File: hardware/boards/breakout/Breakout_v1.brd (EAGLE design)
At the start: 42 x 42 mm, 4 parts

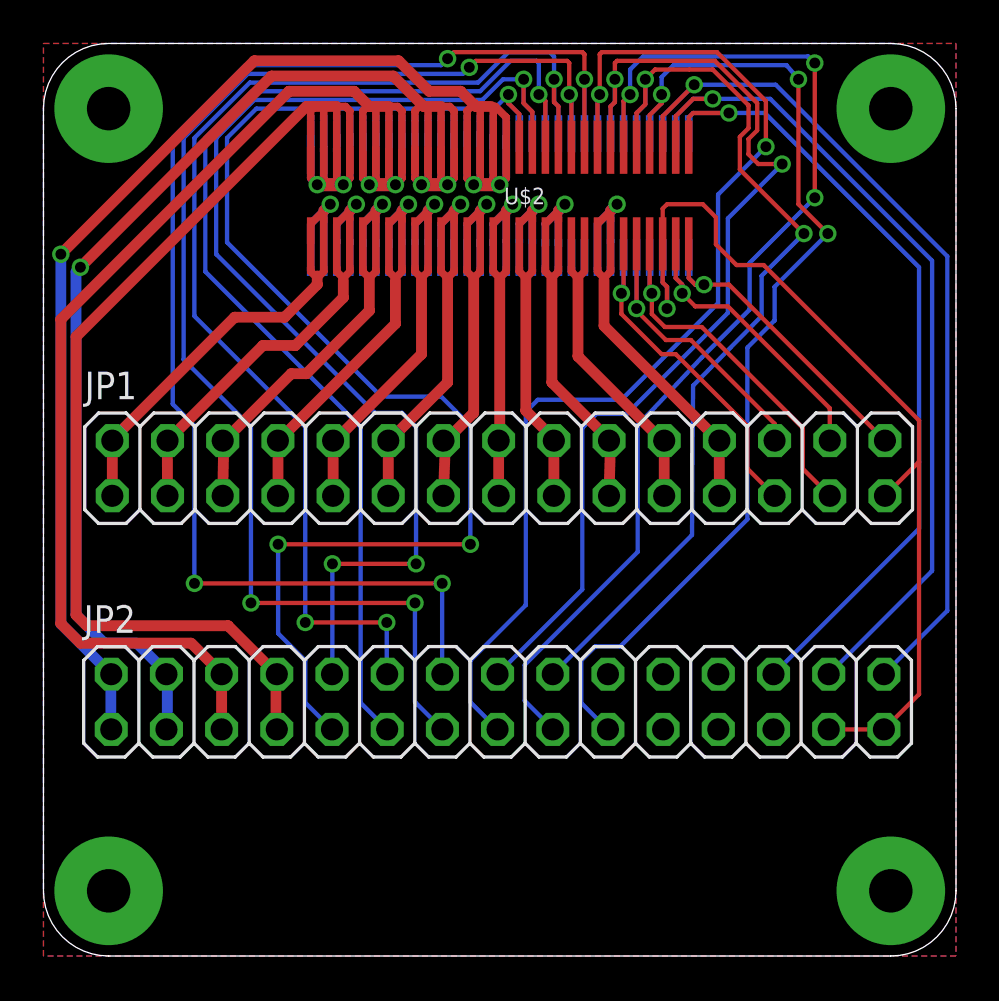
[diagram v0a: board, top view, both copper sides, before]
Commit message: Added V2 breakout ready to order
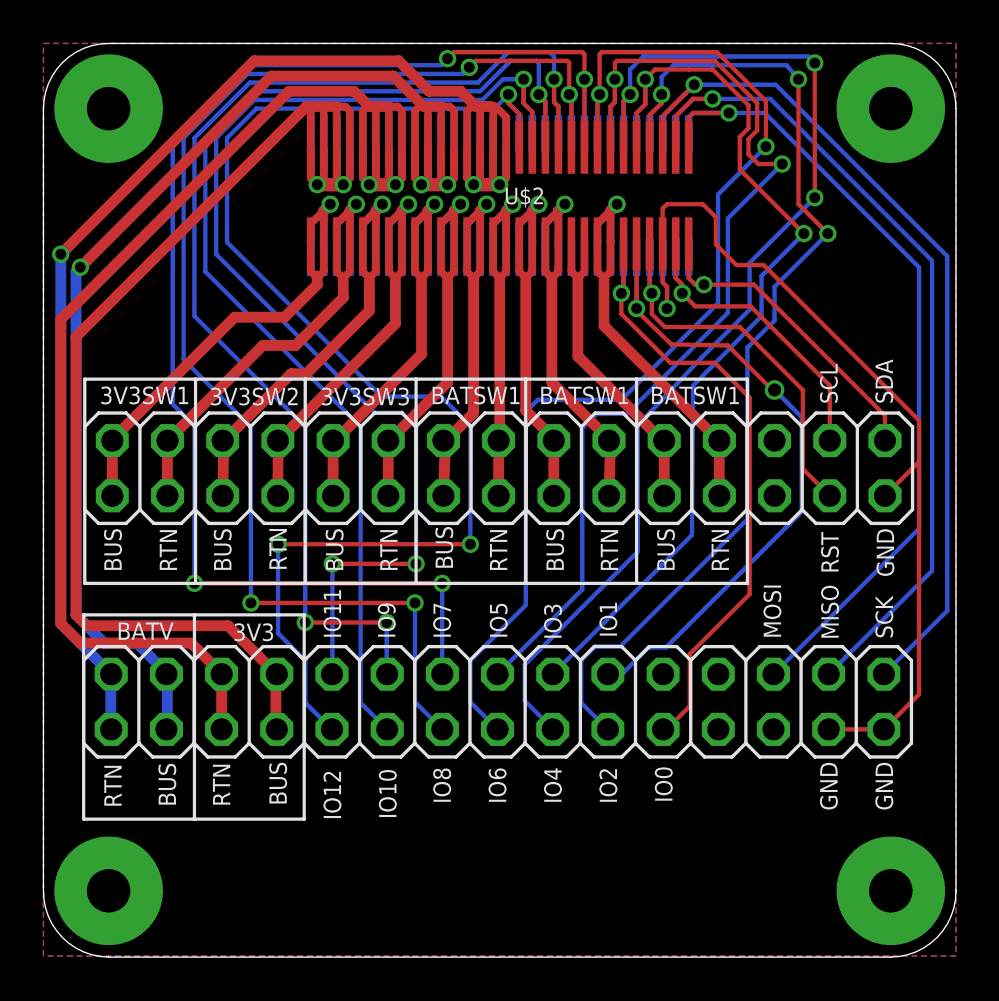
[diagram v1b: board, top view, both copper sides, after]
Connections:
- removed net N$33: JP2.21
- removed net N$43: JP2.20
- net GPIO0: now also JP2.21; no longer JP1.25
- net GPIO1: now also JP2.20; no longer JP1.26
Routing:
- net GPIO1: track 14.7 -> 31.4 mm, vias 1 -> 2
- net GPIO0: track 16.6 -> 29.5 mm
- net /RST: track 17.7 -> 18.7 mm
- net SDA: track 14.5 -> 15.1 mm
- net SCL: track 13.3 -> 13.9 mm
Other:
- board text added: "3V3"
- board text added: "3V3SW1"
- board text added: "3V3SW2"
- board text added: "3V3SW3"
- board text added: "BATSW1"
- board text added: "BATV"
- board text added: "BUS"
- board text added: "GND"
- board text added: "IO0"
- board text added: "IO1"
- board text added: "IO10"
- board text added: "IO11"
- board text added: "IO12"
- board text added: "IO2"
- board text added: "IO3"
- board text added: "IO4"
- board text added: "IO5"
- board text added: "IO6"
- board text added: "IO7"
- board text added: "IO8"
- board text added: "IO9"
- board text added: "MISO"
- board text added: "MOSI"
- board text added: "RST"
- board text added: "RTN"
- board text added: "SCK"
- board text added: "SCL"
- board text added: "SDA"
